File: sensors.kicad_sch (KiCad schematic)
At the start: 0 parts

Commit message: finished v1
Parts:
- added C50: 1uF, symbol Device:C_Small
- added C51: 10uF, symbol Device:C_Small
- added J4: Conn_01x05_Pin, symbol Connector:Conn_01x05_Pin
- added R4, R5: 10k, symbol Device:R_Small_US
- added U3: MMC5983MA, MMC5983MA:PQFN50P300X300X100-16N, symbol MMC5983MA:MMC5983MA
- added U4: BMI088, BMI088:PQFN50P450X300X100-16N, symbol BMI088:BMI088
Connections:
- net LPI2C1_SCL: now also J4.4 (Pin_4), R5.2, U3.1 (SCL/SPI_SCK), U4.8 (SCL/SCK)
- net LPI2C1_SDA: now also J4.3 (Pin_3), R4.2, U3.16 (SDA/SPI_SDI), U4.9 (SDA/SDI)
- new net: C51.1, U3.10 (CAP)
- new net +3.3V: C50.1, J4.2 (Pin_2), R4.1, R5.1, U3.13 (VDDIO), U3.2 (VDD), U3.4 (~{SPI_CS}), U4.11 (VDDIO), U4.3 (VDD), U4.7 (PS)
- new net +5V: J4.1 (Pin_1)
- new net GND: C50.2, C51.2, J4.5 (Pin_5), U3.11 (GND__1), U3.9 (GND), U4.10 (SDO2), U4.15 (SDO1), U4.4 (GNDA), U4.6 (GNDIO)
- no-connect marks 0 -> 9
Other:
- company: (none) -> Northeastern University
- title: (none) -> RT1050 DevBoard for Project Horizon

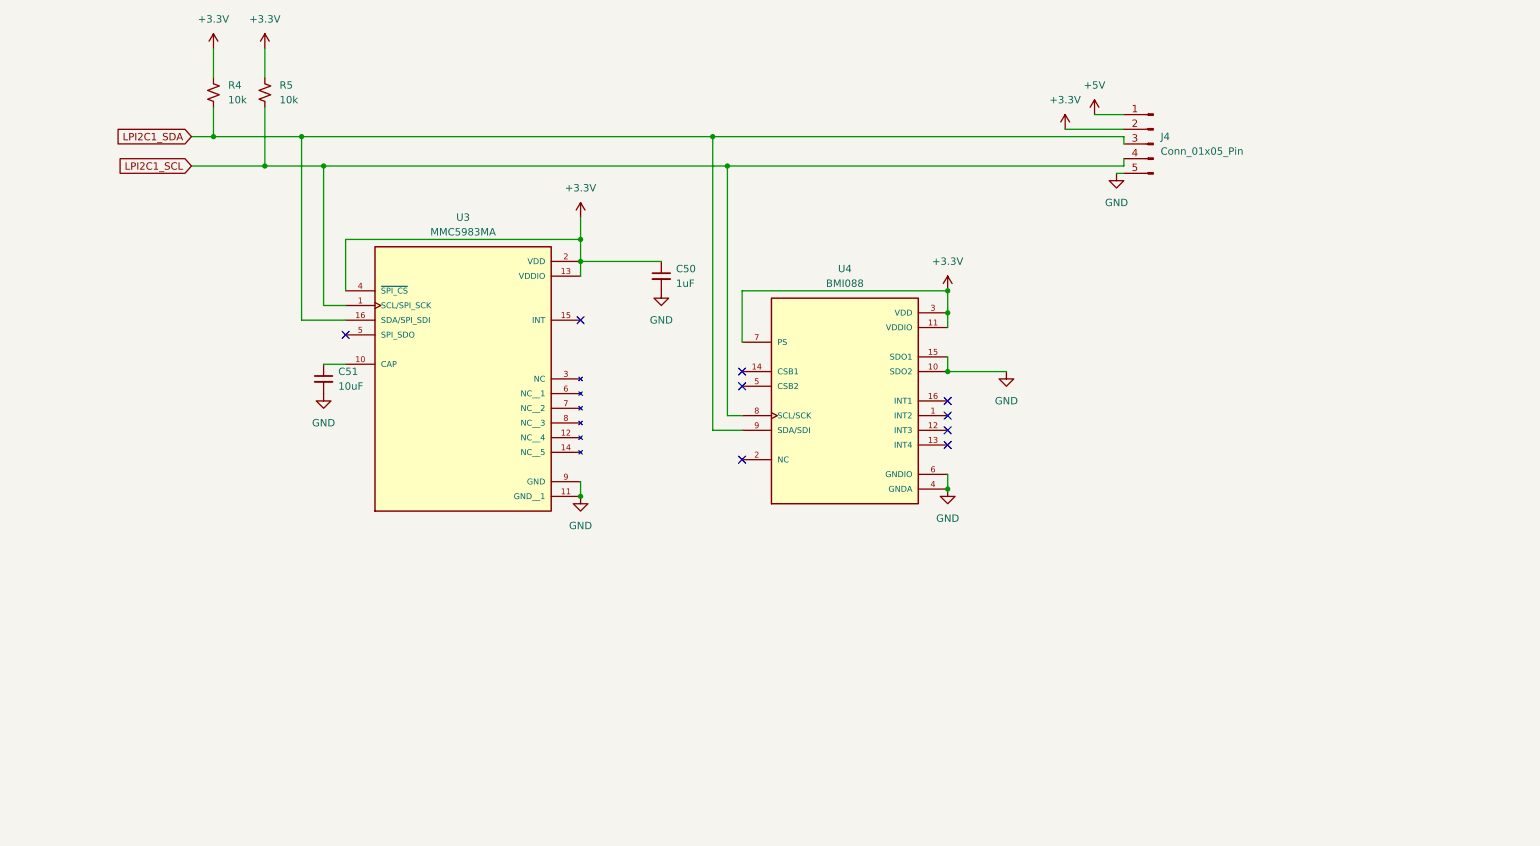
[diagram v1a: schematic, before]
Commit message: added load switches
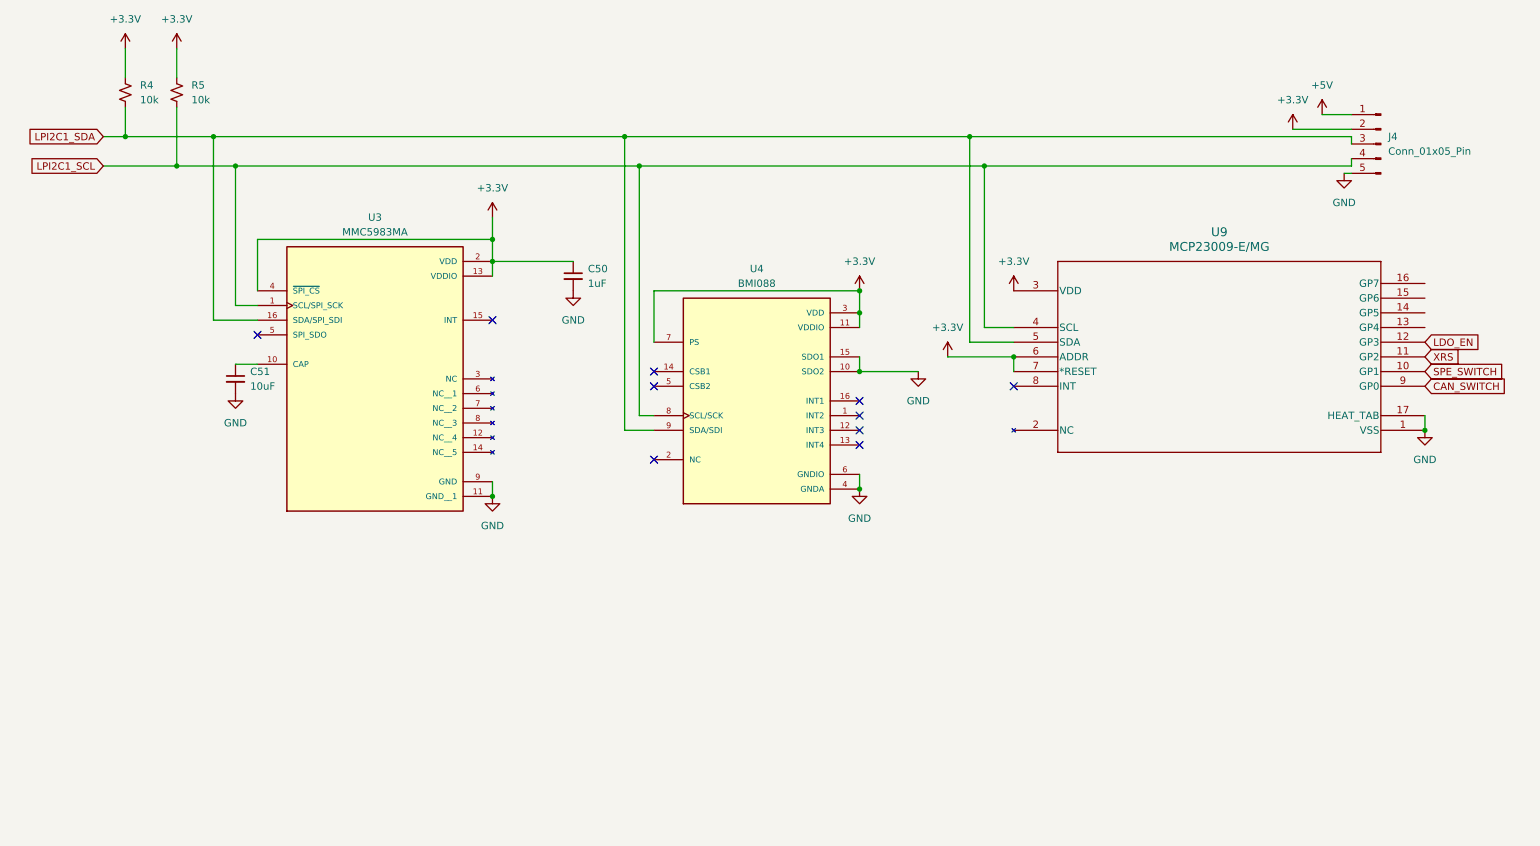
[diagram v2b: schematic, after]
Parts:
- added U9: MCP23009-E/MG, QFN16_3x3MC_MCH, symbol MCP23009-E:MCP23009-E_MG
- C50, C51: footprint (none) -> Capacitor_SMD:C_0402_1005Metric
- J4: footprint (none) -> Connector_PinHeader_2.00mm:PinHeader_1x05_P2.00mm_Vertical
- R4, R5: footprint (none) -> Resistor_SMD:R_0402_1005Metric
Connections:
- net +3.3V: now also U9.3 (VDD), U9.6 (ADDR), U9.7 (*RESET)
- net GND: now also U9.1 (VSS), U9.17 (HEAT_TAB)
- net LPI2C1_SCL: now also U9.4 (SCL)
- net LPI2C1_SDA: now also U9.5 (SDA)
- new net CAN_SWITCH: U9.9 (GP0)
- new net LDO_EN: U9.12 (GP3)
- new net SPE_SWITCH: U9.10 (GP1)
- new net XRS: U9.11 (GP2)
- no-connect marks 9 -> 10
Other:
- moved on the sheet: C50, C51, J4, R4, R5, U3, U4

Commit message: save before sdram redesign
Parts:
- C50, C51: footprint Capacitor_SMD:C_0402_1005Metric -> Capacitor_SMD:C_0201_0603Metric
- J4: symbol Connector:Conn_01x05_Pin -> Connector:Conn_01x04_Pin
- U3: footprint MMC5983MA:PQFN50P300X300X100-16N -> footprints:PQFN50P300X300X100-16N
- U4: footprint BMI088:PQFN50P450X300X100-16N -> footprints:PQFN50P450X300X100-16N
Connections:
- net +5V is gone; now on net +3.3V: J4.1 (Pin_1)
- net +3.3V: no longer J4.2 (Pin_2)
- net GND: now also J4.4 (Pin_4); no longer J4.5 (Pin_5)
- net LDO_EN: now also U9.13 (GP4); no longer U9.12 (GP3)
- net LPI2C1_SCL: now also J4.3 (Pin_3); no longer J4.4 (Pin_4)
- net LPI2C1_SDA: now also J4.2 (Pin_2); no longer J4.3 (Pin_3)
- new net PWDN: U9.12 (GP3)
- no-connect marks 10 -> 13
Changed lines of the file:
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@@
+	)
+	(no_connect
+		(at 260.35 74.93)
+	)
+	(no_connect
+		(at 260.35 77.47)
 	)
 	(no_connect
@@
 	)
 	(no_connect
+		(at 260.35 72.39)
+	)
+	(no_connect
 		(at 127 90.17)
 	)
@@
 		(pts
 			(xy 50.8 46.99) (xy 121.92 46.99)
-		)
-		(stroke
-			(width 0)
-			(type default)
-		)
-	)
-	(wire
-		(pts
-			(xy 242.57 43.18) (xy 247.65 43.18)
 		)
 		(stroke
@@
 		)
 	)
-	(global_label "LDO_EN"
+	(global_label "XRS"
 		(shape input)
-		(at 260.35 82.55 0)
+		(at 260.35 85.09 0)
 		(fields_autoplaced yes)
 		(effects
@@
 		)
 		(property "Intersheetrefs" "${INTERSHEET_REFS}"
-			(at 270.4109 82.55 0)
+			(at 267.0242 85.09 0)
+			(effects
+				(font
+					(size 1.27 1.27)
+				)
+				(justify left)
+				(hide yes)
+			)
+		)
+	)
+	(global_label "PWDN"
+		(shape input)
+		(at 260.35 82.55 0)
+		(fields_autoplaced yes)
+		(effects
+			(font
+				(size 1.27 1.27)
+			)
+			(justify left)
+		)
+		(property "Intersheetrefs" "${INTERSHEET_REFS}"
+			(at 268.6571 82.55 0)
+			(effects
+				(font
+					(size 1.27 1.27)
+				)
+				(justify left)
+				(hide yes)
+			)
+		)
+	)
+	(global_label "LDO_EN"
+		(shape input)
+		(at 260.35 80.01 0)
+		(fields_autoplaced yes)
+		(effects
+			(font
+				(size 1.27 1.27)
+			)
+			(justify left)
+		)
+		(property "Intersheetrefs" "${INTERSHEET_REFS}"
+			(at 270.4109 80.01 0)
 			(effects
 				(font
@@
 				)
 				(justify right)
-				(hide yes)
-			)
-		)
-	)
-	(global_label "XRS"
-		(shape input)
-		(at 260.35 85.09 0)
-		(fields_autoplaced yes)
-		(effects
-			(font
-				(size 1.27 1.27)
-			)
-			(justify left)
-		)
-		(property "Intersheetrefs" "${INTERSHEET_REFS}"
-			(at 267.0242 85.09 0)
-			(effects
-				(font
-					(size 1.27 1.27)
-				)
-				(justify left)
 				(hide yes)
 			)
@@
 			)
 		)
+		(property "Flight" ""
+			(at 189.23 73.66 0)
+			(effects
+				(font
+					(size 1.27 1.27)
+				)
+				(hide yes)
+			)
+		)
+		(property "Proto" ""
+			(at 189.23 73.66 0)
+			(effects
+				(font
+					(size 1.27 1.27)
+				)
+				(hide yes)
+			)
+		)
 		(pin "6"
 		)
@@
 			)
 		)
-		(property "Footprint" "Capacitor_SMD:C_0402_1005Metric"
+		(property "Footprint" "Capacitor_SMD:C_0201_0603Metric"
 			(at 54.61 88.9 0)
 			(effects
@@
 		)
 		(property "Description" "Unpolarized capacitor, small symbol"
+			(at 54.61 88.9 0)
+			(effects
+				(font
+					(size 1.27 1.27)
+				)
+				(hide yes)
+			)
+		)
+		(property "Flight" ""
+			(at 54.61 88.9 0)
+			(effects
+				(font
+					(size 1.27 1.27)
+				)
+				(hide yes)
+			)
+		)
+		(property "Proto" ""
 			(at 54.61 88.9 0)
 			(effects
@@
 			)
 		)
+		(property "Flight" ""
+			(at 35.56 39.37 0)
+			(effects
+				(font
+					(size 1.27 1.27)
+				)
+				(hide yes)
+			)
+		)
+		(property "Proto" ""
+			(at 35.56 39.37 0)
+			(effects
+				(font
+					(size 1.27 1.27)
+				)
+				(hide yes)
+			)
+		)
 		(pin "1"
 		)
@@
 			)
 		)
-		(property "Footprint" "MMC5983MA:PQFN50P300X300X100-16N"
+		(property "Footprint" "footprints:PQFN50P300X300X100-16N"
 			(at 78.74 81.28 0)
 			(effects
@@
 				)
 				(justify bottom)
+				(hide yes)
+			)
+		)
+		(property "Flight" ""
+			(at 78.74 81.28 0)
+			(effects
+				(font
+					(size 1.27 1.27)
+				)
+				(hide yes)
+			)
+		)
+		(property "Proto" ""
+			(at 78.74 81.28 0)
+			(effects
+				(font
+					(size 1.27 1.27)
+				)
 				(hide yes)
 			)
@@
 			)
 		)
-		(property "Footprint" "BMI088:PQFN50P450X300X100-16N"
+		(property "Footprint" "footprints:PQFN50P450X300X100-16N"
 			(at 144.78 92.71 0)
 			(effects
@@
 				)
 				(justify bottom)
+				(hide yes)
+			)
+		)
+		(property "Flight" ""
+			(at 144.78 92.71 0)
+			(effects
+				(font
+					(size 1.27 1.27)
+				)
+				(hide yes)
+			)
+		)
+		(property "Proto" ""
+			(at 144.78 92.71 0)
+			(effects
+				(font
+					(size 1.27 1.27)
+				)
 				(hide yes)
 			)
@@
 			)
 		)
+		(property "Flight" ""
+			(at 44.45 39.37 0)
+			(effects
+				(font
+					(size 1.27 1.27)
+				)
+				(hide yes)
+			)
+		)
+		(property "Proto" ""
+			(at 44.45 39.37 0)
+			(effects
+				(font
+					(size 1.27 1.27)
+				)
+				(hide yes)
+			)
+		)
 		(pin "1"
 		)
@@
 			)
 		)
-		(property "Footprint" "Capacitor_SMD:C_0402_1005Metric"
+		(property "Footprint" "Capacitor_SMD:C_0201_0603Metric"
 			(at 113.03 71.12 0)
 			(effects
@@
 		)
 		(property "Description" "Unpolarized capacitor, small symbol"
+			(at 113.03 71.12 0)
+			(effects
+				(font
+					(size 1.27 1.27)
+				)
+				(hide yes)
+			)
+		)
+		(property "Flight" ""
+			(at 113.03 71.12 0)
+			(effects
+				(font
+					(size 1.27 1.27)
+				)
+				(hide yes)
+			)
+		)
+		(property "Proto" ""
 			(at 113.03 71.12 0)
 			(effects
@@
 	)
 	(symbol
-		(lib_id "Connector:Conn_01x05_Pin")
+		(lib_id "Connector:Conn_01x04_Pin")
 		(at 252.73 48.26 0)
 		(mirror y)
@@
 		(fields_autoplaced yes)
 		(property "Reference" "J4"
-			(at 254 46.9899 0)
+			(at 254 48.2599 0)
 			(effects
 				(font
@@
 		)
 		(property "Value" "Conn_01x05_Pin"
-			(at 254 49.5299 0)
+			(at 254 50.7999 0)
 			(effects
 				(font
@@
 			)
 		)
-		(property "Description" "Generic connector, single row, 01x05, script generated"
+		(property "Description" "Generic connector, single row, 01x04, script generated"
 			(at 252.73 48.26 0)
 			(effects
@@
 			)
 		)
+		(property "Flight" ""
+			(at 252.73 48.26 0)
+			(effects
+				(font
+					(size 1.27 1.27)
+				)
+				(hide yes)
+			)
+		)
+		(property "Proto" ""
+			(at 252.73 48.26 0)
+			(effects
+				(font
+					(size 1.27 1.27)
+				)
+				(hide yes)
+			)
+		)
 		(pin "3"
 		)
@@
 		)
 		(pin "1"
-		)
-		(pin "5"
 		)
 		(instances
@@
 					(unit 1)
 				)
-			)
-		)
-	)
-	(symbol
-		(lib_id "power:+5V")
-		(at 242.57 43.18 0)
-		(unit 1)
-		(exclude_from_sim no)
-		(in_bom yes)
-		(on_board yes)
-		(dnp no)
-		(fields_autoplaced yes)
-		(property "Reference" "#PWR080"
-			(at 242.57 46.99 0)
-			(effects
-				(font
-					(size 1.27 1.27)
-				)
-				(hide yes)
-			)
-		)
-		(property "Value" "+5V"
-			(at 242.57 38.1 0)
-			(effects
-				(font
-					(size 1.27 1.27)
-				)
-			)
-		)
-		(property "Footprint" ""
-			(at 242.57 43.18 0)
-			(effects
-				(font
-					(size 1.27 1.27)
-				)
-				(hide yes)
-			)
-		)
-		(property "Datasheet" ""
-			(at 242.57 43.18 0)
-			(effects
-				(font
-					(size 1.27 1.27)
-				)
-				(hide yes)
-			)
-		)
-		(property "Description" "Power symbol creates a global label with name \"+5V\""
-			(at 242.57 43.18 0)
-			(effects
-				(font
-					(size 1.27 1.27)
-				)
-				(hide yes)
-			)
-		)
-		(pin "1"
-		)
-		(instances
-			(project "RT1050"
-				(path "/dd9d031d-43a1-4442-b493-27451a14e0d9/2d6e0293-1e7f-4e64-b0be-64f8e31d184d"
-					(reference "#PWR080")
-					(unit 1)
-				)

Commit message: SDRAM redo and finished boards
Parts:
- J4: footprint Connector_PinHeader_2.00mm:PinHeader_1x05_P2.00mm_Vertical -> Connector_PinHeader_2.00mm:PinHeader_1x04_P2.00mm_Vertical
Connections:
- net SHDN: now reaches U9.14 (GP5)
- no-connect marks 13 -> 12
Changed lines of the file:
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@@
-	)
-	(no_connect
-		(at 260.35 77.47)
 	)
 	(no_connect
@@
 				)
 				(justify left)
+				(hide yes)
+			)
+		)
+	)
+	(global_label "SHDN"
+		(shape input)
+		(at 260.35 77.47 0)
+		(effects
+			(font
+				(size 1.27 1.27)
+			)
+			(justify left)
+		)
+		(property "Intersheetrefs" "${INTERSHEET_REFS}"
+			(at 260.35 77.47 0)
+			(effects
+				(font
+					(size 1.27 1.27)
+				)
 				(hide yes)
 			)
@@
 			)
 		)
-		(property "Footprint" "Connector_PinHeader_2.00mm:PinHeader_1x05_P2.00mm_Vertical"
+		(property "Footprint" "Connector_PinHeader_2.00mm:PinHeader_1x04_P2.00mm_Vertical"
 			(at 252.73 48.26 0)
 			(effects

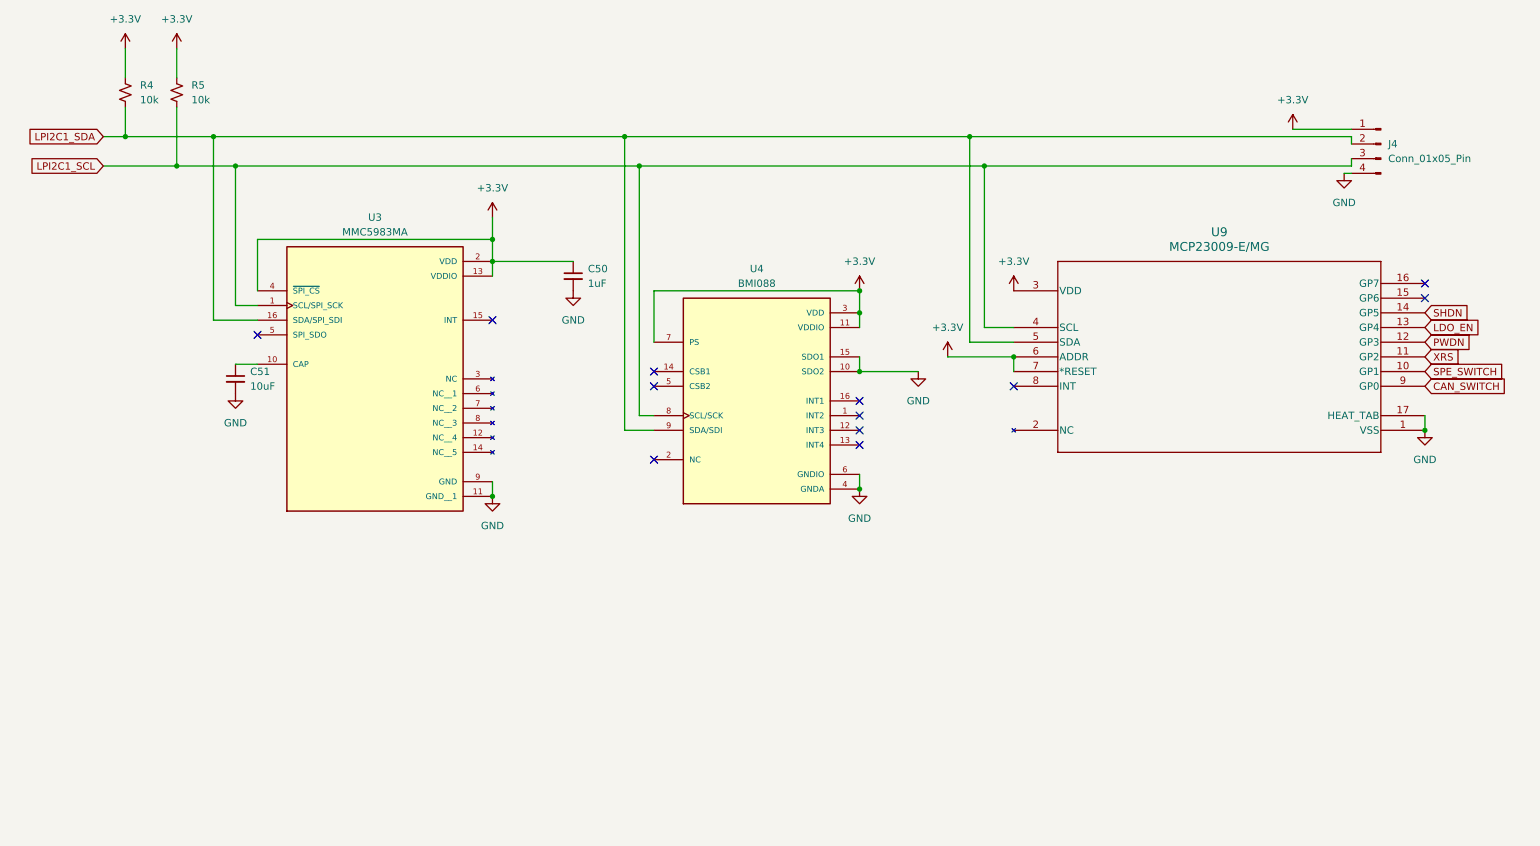
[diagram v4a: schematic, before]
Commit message: added FRAM
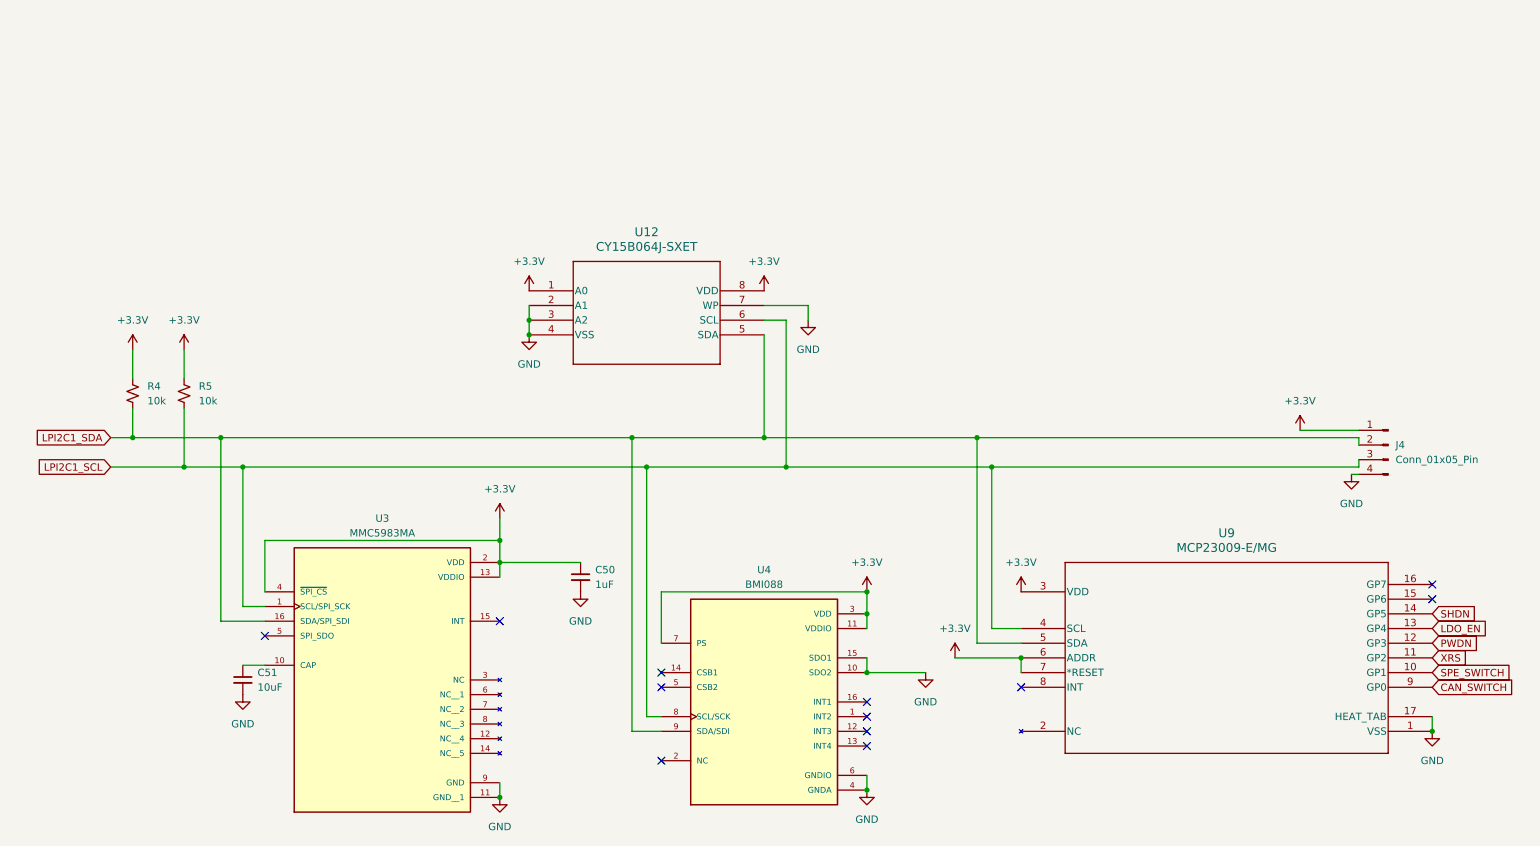
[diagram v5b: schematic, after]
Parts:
- added U12: CY15B064J-SXET, footprints:SO8_CY15_CYP, symbol CY15B064J-SXET:CY15B064J-SXET
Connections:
- net +3.3V: now also U12.1 (A0), U12.8 (VDD)
- net GND: now also U12.2 (A1), U12.3 (A2), U12.4 (VSS), U12.7 (WP)
- net LPI2C1_SCL: now also U12.6 (SCL)
- net LPI2C1_SDA: now also U12.5 (SDA)
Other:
- moved on the sheet: C50, C51, J4, R4, R5, U3, U4, U9
